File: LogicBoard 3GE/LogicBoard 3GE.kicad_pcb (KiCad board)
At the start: 4 copper layers, 103.1 x 140 mm, 161 parts, among them IC201 2363, IC202 74LS00, IC203 74LS32, IC204 2114, IC205 2114, IC206 68A09, IC207 6522, IC208 AY3-8912, IC301 MC1408, IC302 CD4052B, IC303 LF347, IC304 LF353, IC305 4066, J201 CART, J202 MD-90SM, J203 MD-90SM, J204 Power, J301 Video, J302 Audio, J304 Conn_01x03_Pin, Q301 FMMT3905, Q302 FMMT3905, Q303 FMMT3904, SW201 Reset, Y201 6MHz

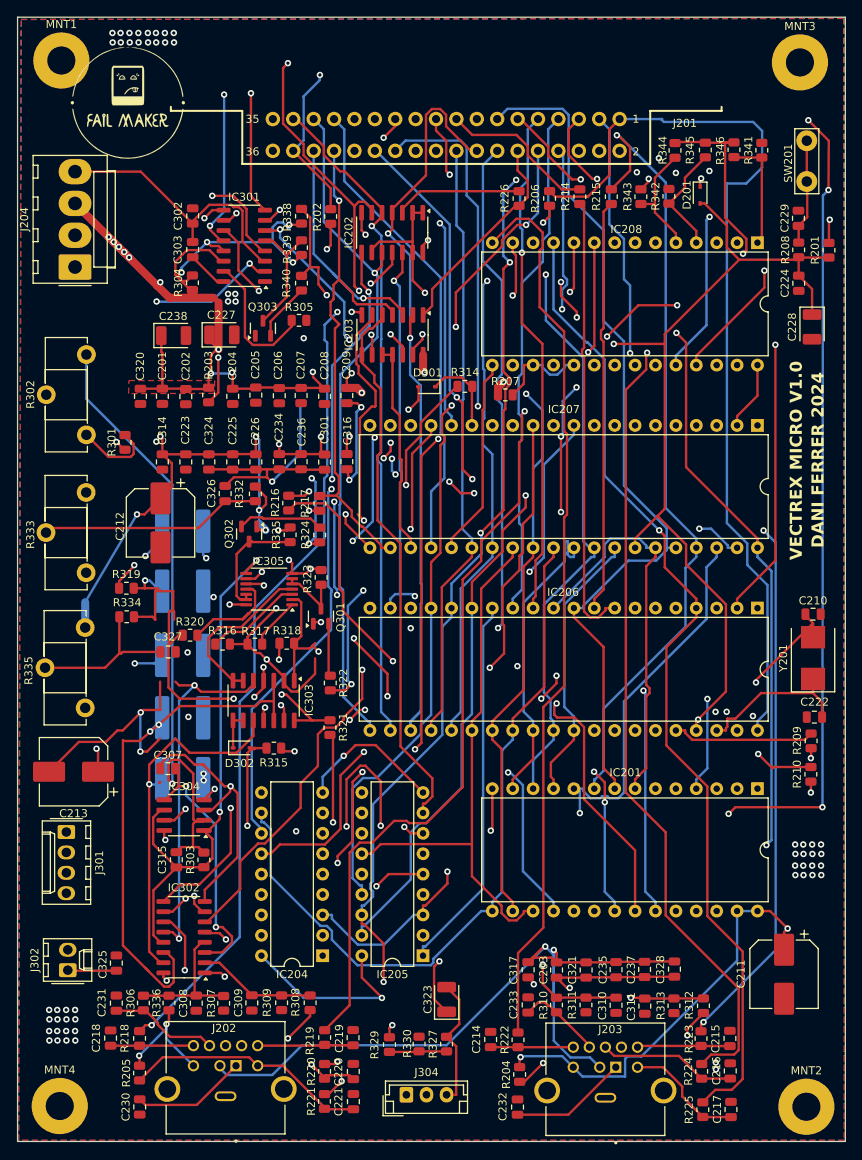
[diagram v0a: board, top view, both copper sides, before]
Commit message: added lm386 audio circuit
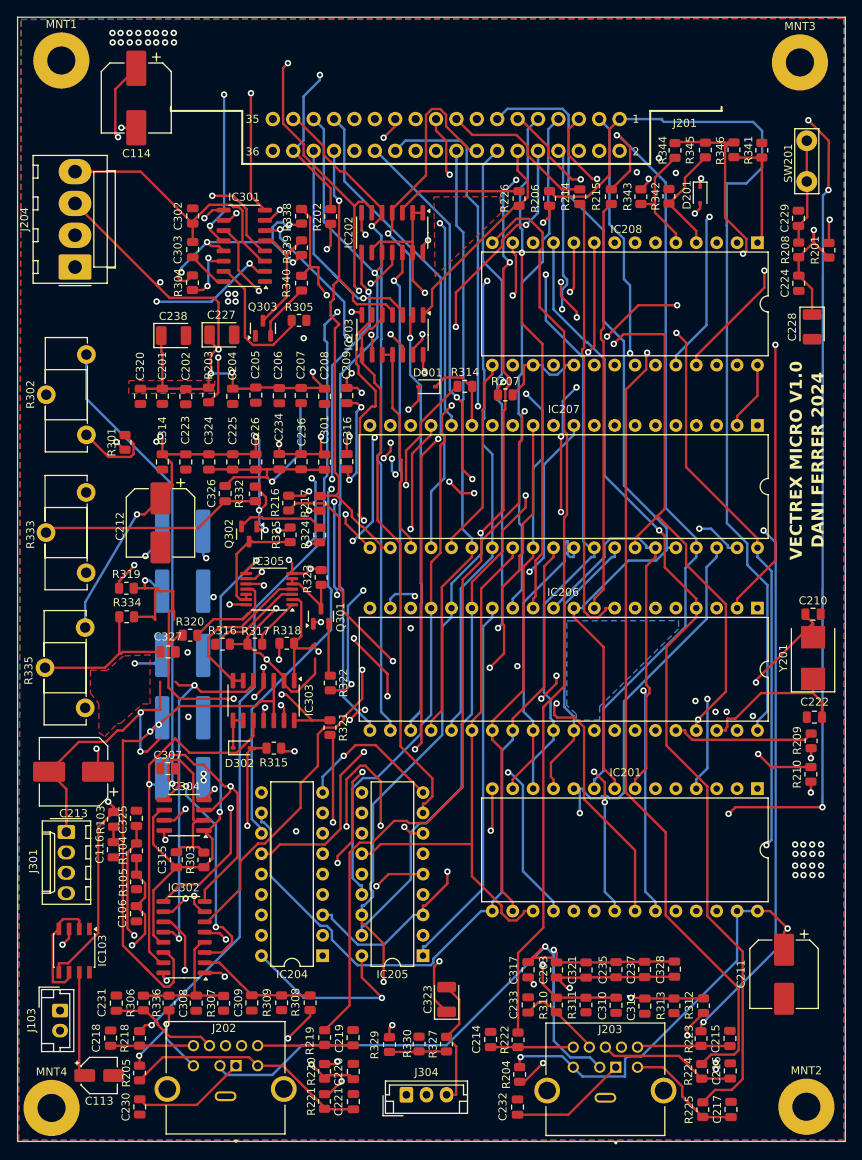
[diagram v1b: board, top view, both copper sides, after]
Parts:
- removed J302: Audio, Connector_Molex:Molex_KK-254_AE-6410-02A_1x02_P2.54mm_Vertical
- removed REF**: FailMaker, VectrexLibrary:FailMaker
- added C106: 0.22nF, Capacitor_SMD:C_0805_2012Metric, F.Cu at (63.1, 138.8)
- added C113: 10uF 16V, Capacitor_SMD:CP_Elec_4x5.3, F.Cu at (58.5, 159.0)
- added C114: 220uF 16V, Capacitor_SMD:CP_Elec_8x10.5, F.Cu at (63.1, 37.3)
- added C116: 0.1uF 50V, Capacitor_SMD:C_0805_2012Metric, F.Cu at (60.2, 130.9)
- added IC103: LM386-3, Package_SO:SOIC-8-N7_3.9x4.9mm_P1.27mm, F.Cu at (55.3, 143.4)
- added J103: Conn_01x02, Connector_JST:JST_EH_B2B-EH-A_1x02_P2.50mm_Vertical, F.Cu at (53.6, 150.9)
- added R103: 10, Resistor_SMD:R_0805_2012Metric, F.Cu at (60.2, 127.1)
- added R104: 6.8k, Resistor_SMD:R_0805_2012Metric, F.Cu at (63.1, 131.0)
- added R105: 47k, Resistor_SMD:R_0805_2012Metric, F.Cu at (63.1, 134.9)
- moved C325 18.2 mm to (63.1, 127.0)
- moved MNT4 1.05 mm to (52.5, 163.0)
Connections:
- net /AUDIO renamed Audio
- C201 pad 1: +5V -> /~{RESET}
- C201 pad 2: GND -> +5V
- C202 pad 1: +5V -> /~{RESET}
- C202 pad 2: GND -> +5V
- C203 pad 2: GND -> +5V
- C204 pad 1: +5V -> /~{RESET}
- C204 pad 2: GND -> +5V
- C205 pad 1: +5V -> /~{RESET}
- C205 pad 2: GND -> +5V
- C206 pad 1: +5V -> /~{RESET}
- C206 pad 2: GND -> +5V
- C207 pad 1: +5V -> /~{RESET}
- C207 pad 2: GND -> +5V
- C208 pad 1: GND -> +5V
- C208 pad 2: +5V -> /~{RESET}
- C209 pad 1: +5V -> /~{RESET}
- C209 pad 2: GND -> +5V
- C210 pad 2: GND -> +5V
- C211 pad 1: +5V -> /~{RESET}
- C211 pad 2: GND -> +5V
- C212 pad 1: +5V -> /~{RESET}
- C212 pad 2: GND -> +5V
- C213 pad 2: GND -> +5V
- C214 pad 1: GND -> +5V
- C215 pad 1: GND -> +5V
- C216 pad 1: GND -> +5V
- C217 pad 1: GND -> +5V
- C218 pad 2: GND -> +5V
- C219 pad 2: GND -> +5V
- C220 pad 2: GND -> +5V
- C221 pad 2: GND -> +5V
- C222 pad 2: GND -> +5V
- C223 pad 1: +5V -> /~{RESET}
- C223 pad 2: GND -> +5V
- C224 pad 1: +5V -> /~{RESET}
- C224 pad 2: GND -> +5V
- C225 pad 1: +5V -> /~{RESET}
- C225 pad 2: GND -> +5V
- C226 pad 1: +5V -> /~{RESET}
- C226 pad 2: GND -> +5V
- C227 pad 1: +5V -> /~{RESET}
- C227 pad 2: GND -> +5V
- C228 pad 1: +5V -> /~{RESET}
- C228 pad 2: GND -> +5V
- C229 pad 2: GND -> +5V
- C230 pad 2: GND -> +5V
- C231 pad 2: GND -> +5V
- C232 pad 1: GND -> +5V
- C233 pad 1: GND -> +5V
- C234 pad 1: +5V -> /~{RESET}
- C234 pad 2: GND -> +5V
- C235 pad 2: GND -> +5V
- C236 pad 1: GND -> +5V
- C236 pad 2: +5V -> /~{RESET}
- C237 pad 1: GND -> +5V
- C238 pad 1: +5V -> /~{RESET}
- C238 pad 2: GND -> +5V
- C301 pad 1: GND -> +5V
- C301 pad 2: +5V -> /~{RESET}
- C302 pad 1: GND -> +5V
- C304 pad 2: GND -> +5V
- C305 pad 1: GND -> +5V
- C306 pad 1: GND -> +5V
- C307 pad 1: GND -> +5V
- C308 pad 2: GND -> +5V
- C309 pad 2: GND -> +5V
- C310 pad 2: GND -> +5V
- C311 pad 2: GND -> +5V
- C312 pad 2: +5V -> /~{RESET}
- C314 pad 1: GND -> +5V
- C314 pad 2: +5V -> /~{RESET}
- C316 pad 1: GND -> +5V
- C316 pad 2: +5V -> /~{RESET}
- C317 pad 1: GND -> +5V
- C320 pad 1: GND -> +5V
- C320 pad 2: +5V -> /~{RESET}
- C321 pad 1: GND -> +5V
- C324 pad 1: GND -> +5V
- C324 pad 2: +5V -> /~{RESET}
- C325 pad 1: GND -> +5V
- C326 pad 1: GND -> +5V
- C327 pad 1: GND -> +5V
- C328 pad 1: GND -> +5V
- D201 pad 2: +5V -> /~{RESET}
- D301 pad 2: GND -> +5V
- IC201 pad 1: +5V -> /~{RESET}
- IC201 pad 14: GND -> +5V
- IC201 pad 27: +5V -> /~{RESET}
- IC201 pad 28: +5V -> /~{RESET}
- IC202 pad 7: GND -> +5V
- IC203 pad 14: +5V -> /~{RESET}
- IC203 pad 7: GND -> +5V
- IC204 pad 18: +5V -> /~{RESET}
- IC204 pad 9: GND -> +5V
- IC205 pad 18: +5V -> /~{RESET}
- IC205 pad 9: GND -> +5V
- IC206 pad 1: GND -> +5V
- IC206 pad 37: +5V -> /~{RESET}
- IC206 pad 7: +5V -> /~{RESET}
- IC207 pad 1: GND -> +5V
- IC207 pad 20: +5V -> /~{RESET}
- IC207 pad 34: +5V -> /~{RESET}
- IC208 pad 16: +5V -> /~{RESET}
- IC208 pad 6: GND -> +5V
- IC301 pad 14: +5V -> /VREF+
- IC301 pad 2: GND -> +5V
- IC302 pad 16: +5V -> /~{RESET}
- IC302 pad 8: GND -> +5V
- IC303 pad 2: +5V -> /~{RESET}
- IC303 pad 4: +5V -> /~{RESET}
- IC304 pad 3: GND -> +5V
- IC304 pad 8: +5V -> /~{RESET}
- IC305 pad 14: +5V -> /~{RESET}
- J201 pad 25: GND -> +5V
- J201 pad 27: GND -> +5V
- J201 pad 28: GND -> +5V
- J202 pad 4: GND -> +5V
- J202 pad 6: +5V -> /~{RESET}
- J202 pad S1: GND -> +5V
- J202 pad S2: GND -> +5V
- J202 pad S3: GND -> +5V
- J203 pad 4: GND -> +5V
- J203 pad 6: +5V -> /~{RESET}
- J203 pad S1: GND -> +5V
- J203 pad S2: GND -> +5V
- J203 pad S3: GND -> +5V
- J204 pad 2: GND -> +5V
- J204 pad 3: +5V -> /~{RESET}
- J301 pad 2: +5V -> /~{RESET}
- J304 pad 1: GND -> +5V
- MNT1 pad 1: GND -> +5V
- MNT2 pad 1: GND -> +5V
- MNT3 pad 1: GND -> +5V
- MNT4 pad 1: GND -> +5V
- Q301 pad 1: +5V -> /~{RESET}
- Q302 pad 1: +5V -> /~{RESET}
- Q303 pad 1: GND -> +5V
- R201 pad 2: +5V -> /~{RESET}
- R203 pad 2: +5V -> /~{RESET}
- R204 pad 2: +5V -> /~{RESET}
- R205 pad 1: +5V -> /~{RESET}
- R207 pad 2: +5V -> /~{RESET}
- R208 pad 1: +5V -> /~{RESET}
- R209 pad 1: +5V -> /~{RESET}
- R210 pad 2: +5V -> /~{RESET}
- R301 pad 2: +5V -> /~{RESET}
- R304 pad 1: +5V -> /VREF+
- R305 pad 1: GND -> +5V
- R307 pad 2: GND -> +5V
- R309 pad 2: GND -> +5V
- R311 pad 2: GND -> +5V
- R313 pad 2: GND -> +5V
- R316 pad 1: +5V -> /~{RESET}
- R317 pad 2: +5V -> /~{RESET}
- R318 pad 1: +5V -> /~{RESET}
- R325 pad 2: +5V -> /~{RESET}
- R330 pad 2: GND -> +5V
- R332 pad 1: +5V -> /~{RESET}
- R333 pad 3: +5V -> /~{RESET}
- R335 pad 3: +5V -> /~{RESET}
- R336 pad 1: +5V -> /~{RESET}
- R341 pad 2: GND -> +5V
- R342 pad 2: GND -> +5V
- R343 pad 2: GND -> +5V
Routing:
- net /~{RESET}: track 0.00 -> 771.2 mm, vias 0 -> 42
- net +5V: track 836.5 -> 410.6 mm, vias 53 -> 75
- net GND: track 261.6 -> 0.00 mm, vias 83 -> 0
- net Net-(C114-Pad1): track 0.00 -> 121.7 mm, vias 0 -> 2
- net Net-(J103-Pin_1): track 0.00 -> 116.1 mm, vias 0 -> 1
- net Net-(IC103-+): track 0.00 -> 24.0 mm, vias 0 -> 2
- net Net-(IC103-BYPASS): track 0.00 -> 13.1 mm
- net /VREF+: track 0.00 -> 7.95 mm, vias 0 -> 2
- net Audio: track 57.8 -> 64.4 mm, vias 0 -> 1
- net /P4: track 134.5 -> 129.7 mm
- net Net-(C116-Pad1): track 0.00 -> 1.93 mm
- net /A15: track 96.5 -> 95.4 mm
- added copper zone on B.Cu, net +5V
- removed copper zone on B.Cu, net GND
- removed copper zone on F.Cu, net GND

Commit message: Adjusted rules to JLCPCB Capacities. Solved all DRC Erros and conflicts
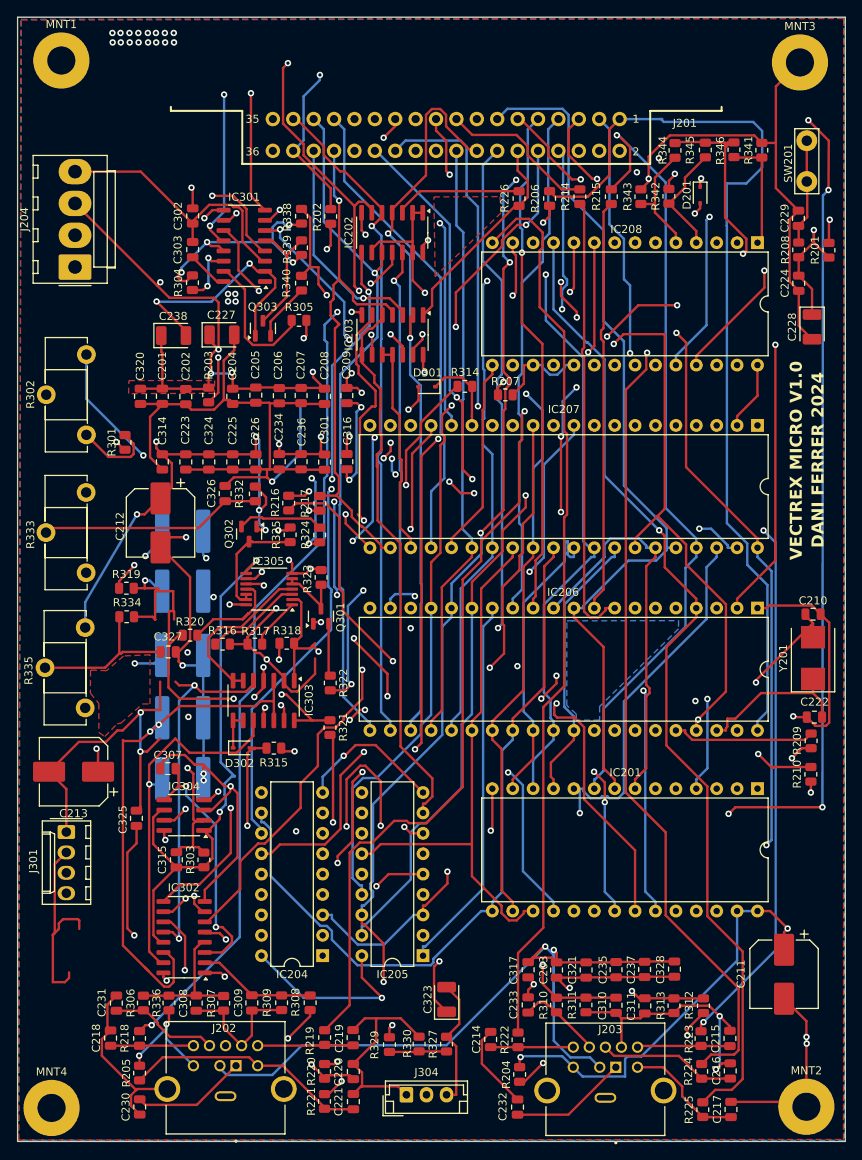
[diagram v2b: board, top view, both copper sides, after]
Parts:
- removed C106: 0.22nF, Capacitor_SMD:C_0805_2012Metric
- removed C113: 10uF 16V, Capacitor_SMD:CP_Elec_4x5.3
- removed C114: 220uF 16V, Capacitor_SMD:CP_Elec_8x10.5
- removed C116: 0.1uF 50V, Capacitor_SMD:C_0805_2012Metric
- removed IC103: LM386-3, Package_SO:SOIC-8-N7_3.9x4.9mm_P1.27mm
- removed J103: Conn_01x02, Connector_JST:JST_EH_B2B-EH-A_1x02_P2.50mm_Vertical
- removed R103: 10, Resistor_SMD:R_0805_2012Metric
- removed R104: 6.8k, Resistor_SMD:R_0805_2012Metric
- removed R105: 47k, Resistor_SMD:R_0805_2012Metric
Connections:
- C201 pad 1: /~{RESET} -> +5V
- C201 pad 2: +5V -> GND
- C202 pad 1: /~{RESET} -> +5V
- C202 pad 2: +5V -> GND
- C203 pad 2: +5V -> GND
- C204 pad 1: /~{RESET} -> +5V
- C204 pad 2: +5V -> GND
- C205 pad 1: /~{RESET} -> +5V
- C205 pad 2: +5V -> GND
- C206 pad 1: /~{RESET} -> +5V
- C206 pad 2: +5V -> GND
- C207 pad 1: /~{RESET} -> +5V
- C207 pad 2: +5V -> GND
- C208 pad 1: +5V -> GND
- C208 pad 2: /~{RESET} -> +5V
- C209 pad 1: /~{RESET} -> +5V
- C209 pad 2: +5V -> GND
- C210 pad 2: +5V -> GND
- C211 pad 1: /~{RESET} -> +5V
- C211 pad 2: +5V -> GND
- C212 pad 1: /~{RESET} -> +5V
- C212 pad 2: +5V -> GND
- C213 pad 2: +5V -> GND
- C214 pad 1: +5V -> GND
- C215 pad 1: +5V -> GND
- C216 pad 1: +5V -> GND
- C217 pad 1: +5V -> GND
- C218 pad 2: +5V -> GND
- C219 pad 2: +5V -> GND
- C220 pad 2: +5V -> GND
- C221 pad 2: +5V -> GND
- C222 pad 2: +5V -> GND
- C223 pad 1: /~{RESET} -> +5V
- C223 pad 2: +5V -> GND
- C224 pad 1: /~{RESET} -> +5V
- C224 pad 2: +5V -> GND
- C225 pad 1: /~{RESET} -> +5V
- C225 pad 2: +5V -> GND
- C226 pad 1: /~{RESET} -> +5V
- C226 pad 2: +5V -> GND
- C227 pad 1: /~{RESET} -> +5V
- C227 pad 2: +5V -> GND
- C228 pad 1: /~{RESET} -> +5V
- C228 pad 2: +5V -> GND
- C229 pad 2: +5V -> GND
- C230 pad 2: +5V -> GND
- C231 pad 2: +5V -> GND
- C232 pad 1: +5V -> GND
- C233 pad 1: +5V -> GND
- C234 pad 1: /~{RESET} -> +5V
- C234 pad 2: +5V -> GND
- C235 pad 2: +5V -> GND
- C236 pad 1: +5V -> GND
- C236 pad 2: /~{RESET} -> +5V
- C237 pad 1: +5V -> GND
- C238 pad 1: /~{RESET} -> +5V
- C238 pad 2: +5V -> GND
- C301 pad 1: +5V -> GND
- C301 pad 2: /~{RESET} -> +5V
- C302 pad 1: +5V -> GND
- C304 pad 2: +5V -> GND
- C305 pad 1: +5V -> GND
- C306 pad 1: +5V -> GND
- C307 pad 1: +5V -> GND
- C308 pad 2: +5V -> GND
- C309 pad 2: +5V -> GND
- C310 pad 2: +5V -> GND
- C311 pad 2: +5V -> GND
- C312 pad 2: /~{RESET} -> +5V
- C314 pad 1: +5V -> GND
- C314 pad 2: /~{RESET} -> +5V
- C316 pad 1: +5V -> GND
- C316 pad 2: /~{RESET} -> +5V
- C317 pad 1: +5V -> GND
- C320 pad 1: +5V -> GND
- C320 pad 2: /~{RESET} -> +5V
- C321 pad 1: +5V -> GND
- C324 pad 1: +5V -> GND
- C324 pad 2: /~{RESET} -> +5V
- C325 pad 1: +5V -> GND
- C326 pad 1: +5V -> GND
- C327 pad 1: +5V -> GND
- C328 pad 1: +5V -> GND
- D201 pad 2: /~{RESET} -> +5V
- D301 pad 2: +5V -> GND
- IC201 pad 1: /~{RESET} -> +5V
- IC201 pad 14: +5V -> GND
- IC201 pad 27: /~{RESET} -> +5V
- IC201 pad 28: /~{RESET} -> +5V
- IC202 pad 7: +5V -> GND
- IC203 pad 14: /~{RESET} -> +5V
- IC203 pad 7: +5V -> GND
- IC204 pad 18: /~{RESET} -> +5V
- IC204 pad 9: +5V -> GND
- IC205 pad 18: /~{RESET} -> +5V
- IC205 pad 9: +5V -> GND
- IC206 pad 1: +5V -> GND
- IC206 pad 37: /~{RESET} -> +5V
- IC206 pad 7: /~{RESET} -> +5V
- IC207 pad 1: +5V -> GND
- IC207 pad 20: /~{RESET} -> +5V
- IC207 pad 34: /~{RESET} -> +5V
- IC208 pad 16: /~{RESET} -> +5V
- IC208 pad 6: +5V -> GND
- IC301 pad 2: +5V -> GND
- IC302 pad 16: /~{RESET} -> +5V
- IC302 pad 8: +5V -> GND
- IC303 pad 2: /~{RESET} -> +5V
- IC303 pad 4: /~{RESET} -> +5V
- IC304 pad 3: +5V -> GND
- IC304 pad 8: /~{RESET} -> +5V
- IC305 pad 14: /~{RESET} -> +5V
- J201 pad 25: +5V -> GND
- J201 pad 27: +5V -> GND
- J201 pad 28: +5V -> GND
- J202 pad 4: +5V -> GND
- J202 pad 6: /~{RESET} -> +5V
- J202 pad S1: +5V -> GND
- J202 pad S2: +5V -> GND
- J202 pad S3: +5V -> GND
- J203 pad 4: +5V -> GND
- J203 pad 6: /~{RESET} -> +5V
- J203 pad S1: +5V -> GND
- J203 pad S2: +5V -> GND
- J203 pad S3: +5V -> GND
- J204 pad 2: +5V -> GND
- J204 pad 3: /~{RESET} -> +5V
- J301 pad 1: +5V -> GND
- J301 pad 2: /~{RESET} -> +5V
- J304 pad 1: +5V -> GND
- MNT1 pad 1: +5V -> GND
- MNT2 pad 1: +5V -> GND
- MNT3 pad 1: +5V -> GND
- MNT4 pad 1: +5V -> GND
- Q301 pad 1: /~{RESET} -> +5V
- Q302 pad 1: /~{RESET} -> +5V
- Q303 pad 1: +5V -> GND
- R201 pad 2: /~{RESET} -> +5V
- R203 pad 2: /~{RESET} -> +5V
- R204 pad 2: /~{RESET} -> +5V
- R205 pad 1: /~{RESET} -> +5V
- R207 pad 2: /~{RESET} -> +5V
- R208 pad 1: /~{RESET} -> +5V
- R209 pad 1: /~{RESET} -> +5V
- R210 pad 2: /~{RESET} -> +5V
- R301 pad 2: /~{RESET} -> +5V
- R305 pad 1: +5V -> GND
- R307 pad 2: +5V -> GND
- R309 pad 2: +5V -> GND
- R311 pad 2: +5V -> GND
- R313 pad 2: +5V -> GND
- R316 pad 1: /~{RESET} -> +5V
- R317 pad 2: /~{RESET} -> +5V
- R318 pad 1: /~{RESET} -> +5V
- R325 pad 2: /~{RESET} -> +5V
- R330 pad 2: +5V -> GND
- R332 pad 1: /~{RESET} -> +5V
- R333 pad 3: /~{RESET} -> +5V
- R335 pad 3: /~{RESET} -> +5V
- R336 pad 1: /~{RESET} -> +5V
- R341 pad 2: +5V -> GND
- R342 pad 2: +5V -> GND
- R343 pad 2: +5V -> GND
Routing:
- net GND: track 0.00 -> 917.7 mm, vias 0 -> 29
- net /~{RESET}: track 771.2 -> 0.00 mm, vias 42 -> 0
- net +5V: track 410.6 -> 964.2 mm, vias 75 -> 74
- net Net-(C114-Pad1): track 121.7 -> 0.00 mm, vias 2 -> 0
- net Net-(J103-Pin_1): track 116.1 -> 0.00 mm, vias 1 -> 0
- net -5VA: track 138.9 -> 163.9 mm
- net Net-(IC103-+): track 24.0 -> 0.00 mm, vias 2 -> 0
- net Net-(IC103-BYPASS): track 13.1 -> 0.00 mm
- net /IOUT: track 123.7 -> 118.2 mm, vias 2 -> 3
- net /~{CARTS}: track 30.8 -> 27.4 mm
- net /VOUT: track 67.9 -> 69.9 mm
- net Net-(C116-Pad1): track 1.93 -> 0.00 mm
- net /A8: track 180.8 -> 182.7 mm
- net /~{RAMS}: track 81.4 -> 82.1 mm
- added copper zone on In2.Cu, net +5V
- added copper zone on B.Cu, net GND
- added copper zone on F.Cu, net GND
